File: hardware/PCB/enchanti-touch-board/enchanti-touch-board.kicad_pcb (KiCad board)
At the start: 2 copper layers, 72.4 x 31.8 mm, 91 parts, among them J2 Progamming Header, U1 CY8C4149AZI-S598

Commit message: rename PCB files to enchantiS3, exposed SPI pins for touch board
Renamed ESP32 board PCB files to EnchantiS3
Exposed SPI pins for enchanti touch board
Changed Aux touch board connector to two 4 pin JST SM connectors
Updated Enchanti touch board BOM an manufacturing files
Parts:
- removed the GPIO3 at (213.3, 75.0)
- added GPIO2: I2C, JST-footprints:JST_SH_BM04B-SRSS-TB_1x04-1MP_P1.00mm_Vertical, F.Cu at (213.6, 70.5)
- added GPIO4: SPI2, JST-footprints:JST_SH_BM04B-SRSS-TB_1x04-1MP_P1.00mm_Vertical, F.Cu at (213.6, 62.6)
- GPIO3: renamed from GPIO2; value INTERRUPT -> SPI1
- moved R63 8.76 mm to (178.9, 53.6)
- moved R1 8.76 mm to (180.0, 54.7)
- moved R2 8.76 mm to (179.2, 54.7)
- moved R64 8.76 mm to (180.3, 53.6)
- moved C5 3.57 mm to (182.7, 54.2)
- moved C4 3.57 mm to (181.8, 54.2)
- renumbered GPIO4 to GPIO5
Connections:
- GPIO3 pad 1: /POLL_AUX -> /CIPO_MAIN
- GPIO3 pad 2: /EVT_AUX -> /SCLK_MAIN
- GPIO3 pad 3: /POLL_MAIN -> /COPI_MAIN
- GPIO3 pad 4: /EVT_MAIN -> /CS_MAIN
- GPIO5 pad 1: /POLL_AUX -> /POLL_MAIN
- GPIO5 pad 2: /EVT_AUX -> /EVT_MAIN
- R1 pad 1: /P30 -> /P40
- R2 pad 1: /P31 -> /P41
- U1 pad 27: /P30 -> unconnected-(U1-P3.0-Pad27)
- U1 pad 28: /P31 -> unconnected-(U1-P3.1-Pad28)
- U1 pad 36: /MOSI -> /COPI_AUX
- U1 pad 37: /MISO -> /CIPO_AUX
- U1 pad 38: /SPICLK -> /SCLK_AUX
- U1 pad 39: /CS -> /CS_AUX
- U1 pad 41: /MSC043 -> unconnected-(U1-P11.5-Pad41)
- U1 pad 43: /CMOD00 -> /P40
- U1 pad 44: /CMOD01 -> /P41
- U1 pad 45: /MSC046 -> /CMOD00
- U1 pad 46: /MSC047 -> /CMOD01
- U1 pad 47: /MSC048 -> /COPI_MAIN
- U1 pad 48: /MSC049 -> /CIPO_MAIN
- U1 pad 49: /MSC050 -> /SCLK_MAIN
- U1 pad 50: /MSC051 -> /CS_MAIN
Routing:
- net /POLL_AUX: track 126.4 -> 0.00 mm, vias 4 -> 0
- net /EVT_AUX: track 123.5 -> 0.00 mm, vias 4 -> 0
- net /CS: track 44.2 -> 0.00 mm, vias 2 -> 0
- net /SPICLK: track 44.0 -> 0.00 mm, vias 2 -> 0
- net /MISO: track 43.7 -> 0.00 mm, vias 2 -> 0
- net /MOSI: track 43.5 -> 0.00 mm, vias 2 -> 0
- net /COPI_MAIN: track 0.00 -> 37.5 mm, vias 0 -> 2
- net /CIPO_MAIN: track 0.00 -> 37.3 mm, vias 0 -> 2
- net /SCLK_MAIN: track 0.00 -> 36.2 mm, vias 0 -> 2
- net /CS_AUX: track 0.00 -> 34.9 mm, vias 0 -> 2
- net /CS_MAIN: track 0.00 -> 34.6 mm, vias 0 -> 2
- net /COPI_AUX: track 0.00 -> 33.3 mm, vias 0 -> 2
- net /SCLK_AUX: track 0.00 -> 32.7 mm, vias 0 -> 2
- net /CIPO_AUX: track 0.00 -> 31.5 mm, vias 0 -> 2
- net +3V3: track 169.0 -> 156.4 mm, vias 10 -> 7
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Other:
- board text added: "Enchanti Touch Board v0.2 IDMIL, McGill University Albert Niyonsenga 2023/12"
- board text added: "HOST BOARD"
- board text added: "Power"
- board text added: "SPI"
- board text removed: "AUX"
- board text removed: "EVT (Main) Poll (Main) EVT (Aux) Poll (Aux)"
- board text removed: "MAIN"
- board text removed: "SPIMODE"
- board text removed: "T-Stick Custom Touch Board v0.1 IDMIL Albert Niyonsenga 2023/11"

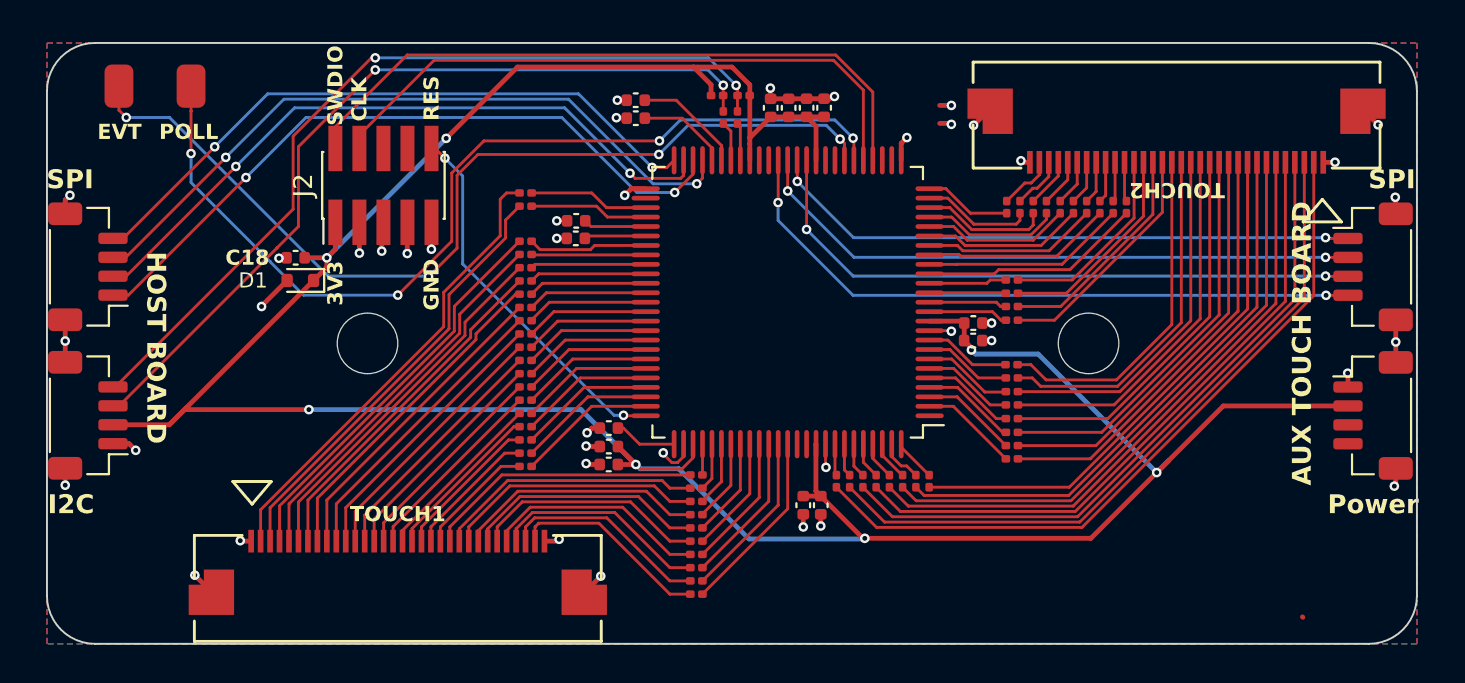
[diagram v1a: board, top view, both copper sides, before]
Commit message: Updated touch sensor design for better fit with assembly, fixed small allignment issue with touch board
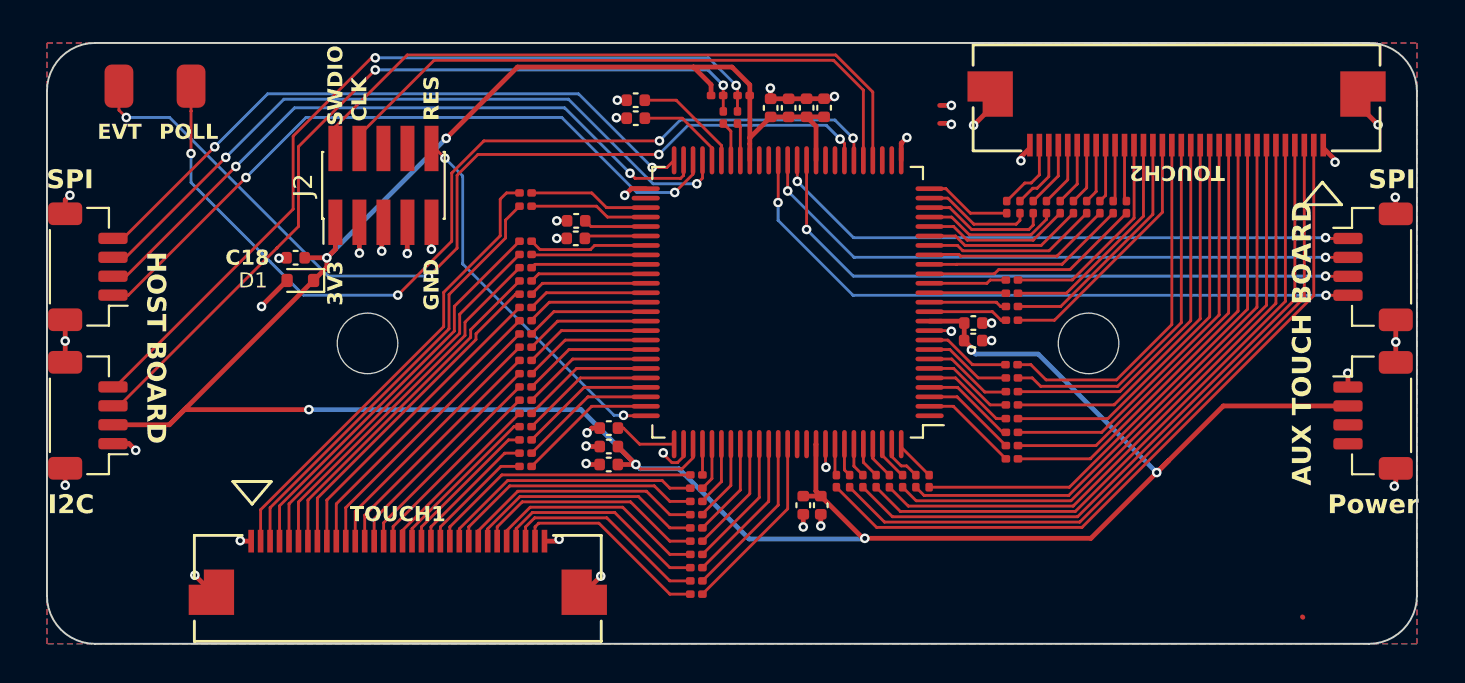
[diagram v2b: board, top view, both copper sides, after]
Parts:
- moved TOUCH2 0.91 mm to (203.2, 53.7)
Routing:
- net /TOUCH004: track 32.7 -> 33.6 mm
- net /TOUCH002: track 35.5 -> 36.4 mm
- net /TOUCH028: track 2.81 -> 3.72 mm
- net /TOUCH027: track 2.60 -> 3.51 mm
- net /TOUCH026: track 2.51 -> 3.42 mm
- net /TOUCH025: track 2.42 -> 3.33 mm
- net /TOUCH024: track 2.34 -> 3.25 mm
- net /TOUCH023: track 2.25 -> 3.16 mm
- net /TOUCH022: track 2.17 -> 3.08 mm
- net /TOUCH021: track 2.09 -> 3.00 mm
- net /TOUCH020: track 2.09 -> 3.00 mm
- net /TOUCH019: track 10.4 -> 11.3 mm
- net /TOUCH018: track 11.2 -> 12.1 mm
- net /TOUCH017: track 11.9 -> 12.8 mm
- net /TOUCH016: track 12.6 -> 13.5 mm
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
